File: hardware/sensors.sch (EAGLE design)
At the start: 29 parts, among them J1 CDH, J2 OW, J3 DBG, J4 SUN-UART, J5 ADCS, J6 ENV, J7 SUN, U1 DS18B20, U2 DS18B20, U3 DS18B20

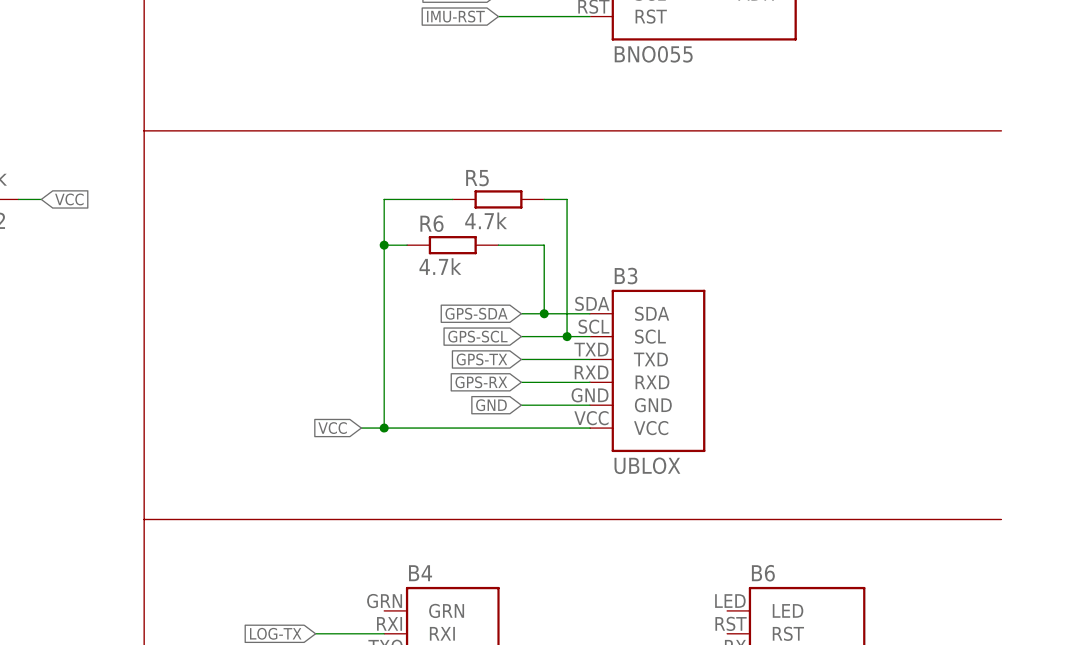
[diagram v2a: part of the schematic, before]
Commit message: Add GPS chip with external antenna
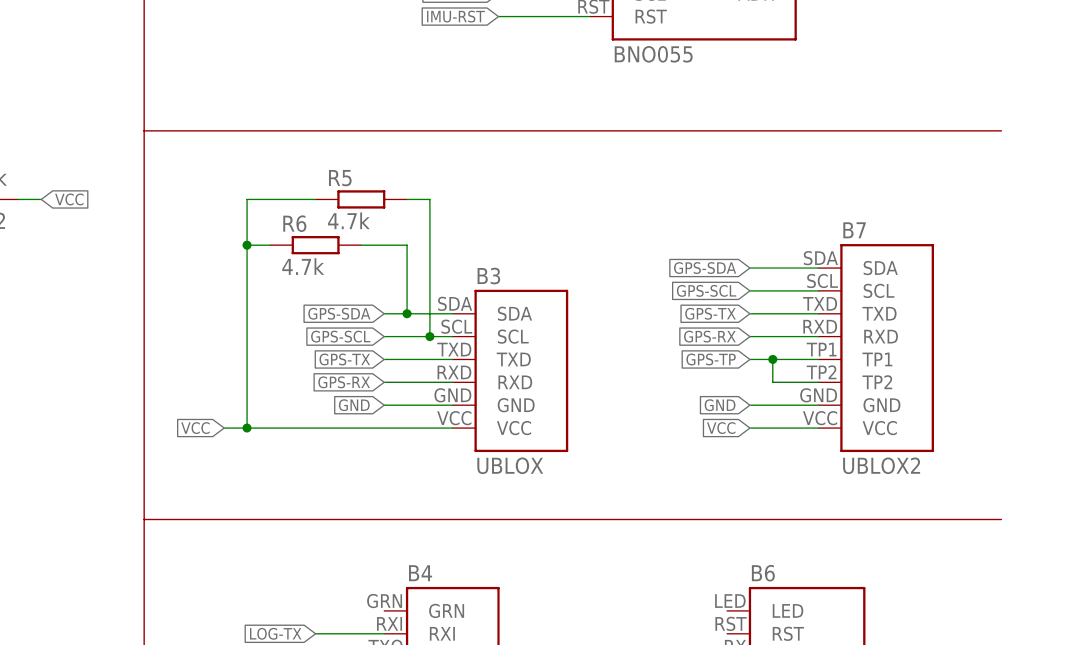
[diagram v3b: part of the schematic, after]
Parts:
- added B7: UBLOX2, Frcy:UPUTRONICS-UBLOX-M8Q
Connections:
- new net GPS-TP: B7.TP1, B7.TP2
- net GND: now also B7.GND
- net GPS-RX: now also B7.RXD
- net GPS-SCL: now also B7.SCL
- net GPS-SDA: now also B7.SDA
- net GPS-TX: now also B7.TXD
- net VCC: now also B7.VCC
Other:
- moved on the sheet: B3, R5, R6
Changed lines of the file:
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@@
 <?xml version="1.0" encoding="utf-8"?>
 <!DOCTYPE eagle SYSTEM "eagle.dtd">
-<eagle version="8.6.0">
+<eagle version="9.0.0">
 <drawing>
 <settings>
@@
 <setting verticaltext="up"/>
 </settings>
-<grid distance="0.1" unitdist="inch" unit="inch" style="lines" multiple="1" display="yes" altdistance="0.05" altunitdist="inch" altunit="inch"/>
+<grid distance="0.1" unitdist="inch" unit="inch" style="lines" multiple="1" display="no" altdistance="0.01" altunitdist="inch" altunit="inch"/>
 <layers>
 <layer number="1" name="Top" color="4" fill="1" visible="no" active="no"/>
@@
 <part name="C10" library="rcl" library_urn="urn:adsk.eagle:library:334" deviceset="C-EU" device="C2012" package3d_urn="urn:adsk.eagle:package:23625/2" value="0.1uF"/>
 <part name="B6" library="Frcy" deviceset="HUAMAO-HM-11" device="BO"/>
+<part name="B7" library="Frcy" deviceset="UPUTRONICS-UBLOX-M8Q" device="" value="UBLOX2"/>
 </parts>
 <sheets>
@@
 <instance part="P+1" gate="VCC" x="144.78" y="33.02"/>
 <instance part="GND1" gate="1" x="144.78" y="17.78"/>
-<instance part="B3" gate="G$1" x="215.9" y="109.22"/>
+<instance part="B3" gate="G$1" x="200.66" y="109.22"/>
 <instance part="B4" gate="G$1" x="195.58" y="76.2"/>
 <instance part="J2" gate="G$1" x="15.24" y="53.34" rot="MR0"/>
@@
 </instance>
 <instance part="U3" gate="G$1" x="43.18" y="116.84"/>
-<instance part="R5" gate="G$1" x="200.66" y="129.54"/>
-<instance part="R6" gate="G$1" x="195.58" y="124.46"/>
+<instance part="R5" gate="G$1" x="185.42" y="129.54"/>
+<instance part="R6" gate="G$1" x="180.34" y="124.46"/>
 <instance part="C1" gate="G$1" x="25.4" y="86.36" rot="R90"/>
 <instance part="C2" gate="G$1" x="25.4" y="58.42" rot="R90"/>
@@
 <instance part="C10" gate="G$1" x="15.24" y="111.76"/>
 <instance part="B6" gate="G$1" x="233.68" y="78.74"/>
+<instance part="B7" gate="G$1" x="241.3" y="114.3"/>
 </instances>
 <busses>
@@
 <segment>
 <pinref part="B3" gate="G$1" pin="VCC"/>
-<wire x1="210.82" y1="104.14" x2="187.96" y2="104.14" width="0.1524" layer="91"/>
-<label x="185.42" y="104.14" size="1.27" layer="95" rot="R180" xref="yes"/>
-<wire x1="187.96" y1="104.14" x2="185.42" y2="104.14" width="0.1524" layer="91"/>
-<wire x1="187.96" y1="104.14" x2="187.96" y2="124.46" width="0.1524" layer="91"/>
-<junction x="187.96" y="104.14"/>
+<wire x1="195.58" y1="104.14" x2="172.72" y2="104.14" width="0.1524" layer="91"/>
+<label x="170.18" y="104.14" size="1.27" layer="95" rot="R180" xref="yes"/>
+<wire x1="172.72" y1="104.14" x2="170.18" y2="104.14" width="0.1524" layer="91"/>
+<wire x1="172.72" y1="104.14" x2="172.72" y2="124.46" width="0.1524" layer="91"/>
+<junction x="172.72" y="104.14"/>
 <pinref part="R6" gate="G$1" pin="1"/>
-<wire x1="187.96" y1="124.46" x2="190.5" y2="124.46" width="0.1524" layer="91"/>
-<wire x1="187.96" y1="124.46" x2="187.96" y2="129.54" width="0.1524" layer="91"/>
-<junction x="187.96" y="124.46"/>
+<wire x1="172.72" y1="124.46" x2="175.26" y2="124.46" width="0.1524" layer="91"/>
+<wire x1="172.72" y1="124.46" x2="172.72" y2="129.54" width="0.1524" layer="91"/>
+<junction x="172.72" y="124.46"/>
 <pinref part="R5" gate="G$1" pin="1"/>
-<wire x1="187.96" y1="129.54" x2="195.58" y2="129.54" width="0.1524" layer="91"/>
+<wire x1="172.72" y1="129.54" x2="180.34" y2="129.54" width="0.1524" layer="91"/>
 </segment>
 <segment>
@@
 <label x="218.44" y="71.12" size="1.27" layer="95" rot="R180" xref="yes"/>
 </segment>
+<segment>
+<wire x1="236.22" y1="104.14" x2="228.6" y2="104.14" width="0.1524" layer="91"/>
+<label x="228.6" y="104.14" size="1.27" layer="95" rot="R180" xref="yes"/>
+<pinref part="B7" gate="G$1" pin="VCC"/>
+</segment>
 </net>
 <net name="GND" class="0">
@@
 <segment>
 <pinref part="B3" gate="G$1" pin="GND"/>
-<wire x1="210.82" y1="106.68" x2="203.2" y2="106.68" width="0.1524" layer="91"/>
-<label x="203.2" y="106.68" size="1.27" layer="95" rot="R180" xref="yes"/>
+<wire x1="195.58" y1="106.68" x2="187.96" y2="106.68" width="0.1524" layer="91"/>
+<label x="187.96" y="106.68" size="1.27" layer="95" rot="R180" xref="yes"/>
 </segment>
 <segment>
@@
 <label x="218.44" y="73.66" size="1.27" layer="95" rot="R180" xref="yes"/>
 </segment>
+<segment>
+<wire x1="236.22" y1="106.68" x2="228.6" y2="106.68" width="0.1524" layer="91"/>
+<label x="228.6" y="106.68" size="1.27" layer="95" rot="R180" xref="yes"/>
+<pinref part="B7" gate="G$1" pin="GND"/>
+</segment>
 </net>
 <net name="IMU-SDA" class="0">
@@
 <segment>
 <pinref part="B3" gate="G$1" pin="SDA"/>
-<wire x1="210.82" y1="116.84" x2="205.74" y2="116.84" width="0.1524" layer="91"/>
-<label x="203.2" y="116.84" size="1.27" layer="95" rot="R180" xref="yes"/>
+<wire x1="195.58" y1="116.84" x2="190.5" y2="116.84" width="0.1524" layer="91"/>
+<label x="187.96" y="116.84" size="1.27" layer="95" rot="R180" xref="yes"/>
 <pinref part="R6" gate="G$1" pin="2"/>
-<wire x1="205.74" y1="116.84" x2="203.2" y2="116.84" width="0.1524" layer="91"/>
-<wire x1="200.66" y1="124.46" x2="205.74" y2="124.46" width="0.1524" layer="91"/>
-<wire x1="205.74" y1="124.46" x2="205.74" y2="116.84" width="0.1524" layer="91"/>
-<junction x="205.74" y="116.84"/>
+<wire x1="190.5" y1="116.84" x2="187.96" y2="116.84" width="0.1524" layer="91"/>
+<wire x1="185.42" y1="124.46" x2="190.5" y2="124.46" width="0.1524" layer="91"/>
+<wire x1="190.5" y1="124.46" x2="190.5" y2="116.84" width="0.1524" layer="91"/>
+<junction x="190.5" y="116.84"/>
 </segment>
 <segment>
@@
 <label x="88.9" y="119.38" size="1.27" layer="95" rot="R180" xref="yes"/>
 </segment>
+<segment>
+<wire x1="236.22" y1="121.92" x2="228.6" y2="121.92" width="0.1524" layer="91"/>
+<label x="228.6" y="121.92" size="1.27" layer="95" rot="R180" xref="yes"/>
+<pinref part="B7" gate="G$1" pin="SDA"/>
+</segment>
 </net>
 <net name="GPS-SCL" class="0">
 <segment>
 <pinref part="B3" gate="G$1" pin="SCL"/>
-<wire x1="210.82" y1="114.3" x2="208.28" y2="114.3" width="0.1524" layer="91"/>
-<label x="203.2" y="114.3" size="1.27" layer="95" rot="R180" xref="yes"/>
+<wire x1="195.58" y1="114.3" x2="193.04" y2="114.3" width="0.1524" layer="91"/>
+<label x="187.96" y="114.3" size="1.27" layer="95" rot="R180" xref="yes"/>
 <pinref part="R5" gate="G$1" pin="2"/>
-<wire x1="208.28" y1="114.3" x2="203.2" y2="114.3" width="0.1524" layer="91"/>
-<wire x1="205.74" y1="129.54" x2="208.28" y2="129.54" width="0.1524" layer="91"/>
-<wire x1="208.28" y1="129.54" x2="208.28" y2="114.3" width="0.1524" layer="91"/>
-<junction x="208.28" y="114.3"/>
+<wire x1="193.04" y1="114.3" x2="187.96" y2="114.3" width="0.1524" layer="91"/>
+<wire x1="190.5" y1="129.54" x2="193.04" y2="129.54" width="0.1524" layer="91"/>
+<wire x1="193.04" y1="129.54" x2="193.04" y2="114.3" width="0.1524" layer="91"/>
+<junction x="193.04" y="114.3"/>
 </segment>
 <segment>
@@
 <wire x1="96.52" y1="116.84" x2="88.9" y2="116.84" width="0.1524" layer="91"/>
 <label x="88.9" y="116.84" size="1.27" layer="95" rot="R180" xref="yes"/>
+</segment>
+<segment>
+<label x="228.6" y="119.38" size="1.27" layer="95" rot="R180" xref="yes"/>
+<wire x1="236.22" y1="119.38" x2="228.6" y2="119.38" width="0.1524" layer="91"/>
+<pinref part="B7" gate="G$1" pin="SCL"/>
 </segment>
 </net>
@@
 <segment>
 <pinref part="B3" gate="G$1" pin="TXD"/>
-<wire x1="210.82" y1="111.76" x2="203.2" y2="111.76" width="0.1524" layer="91"/>
-<label x="203.2" y="111.76" size="1.27" layer="95" rot="R180" xref="yes"/>
+<wire x1="195.58" y1="111.76" x2="187.96" y2="111.76" width="0.1524" layer="91"/>
+<label x="187.96" y="111.76" size="1.27" layer="95" rot="R180" xref="yes"/>
 </segment>
 <segment>
@@
 <label x="76.2" y="53.34" size="1.27" layer="95" xref="yes"/>
 </segment>
+<segment>
+<wire x1="236.22" y1="116.84" x2="228.6" y2="116.84" width="0.1524" layer="91"/>
+<label x="228.6" y="116.84" size="1.27" layer="95" rot="R180" xref="yes"/>
+<pinref part="B7" gate="G$1" pin="TXD"/>
+</segment>
 </net>
 <net name="GPS-RX" class="0">
 <segment>
 <pinref part="B3" gate="G$1" pin="RXD"/>
-<wire x1="210.82" y1="109.22" x2="203.2" y2="109.22" width="0.1524" layer="91"/>
-<label x="203.2" y="109.22" size="1.27" layer="95" rot="R180" xref="yes"/>
+<wire x1="195.58" y1="109.22" x2="187.96" y2="109.22" width="0.1524" layer="91"/>
+<label x="187.96" y="109.22" size="1.27" layer="95" rot="R180" xref="yes"/>
 </segment>
 <segment>
@@
 <label x="76.2" y="55.88" size="1.27" layer="95" xref="yes"/>
 </segment>
+<segment>
+<wire x1="236.22" y1="114.3" x2="228.6" y2="114.3" width="0.1524" layer="91"/>
+<label x="228.6" y="114.3" size="1.27" layer="95" rot="R180" xref="yes"/>
+<pinref part="B7" gate="G$1" pin="RXD"/>
+</segment>
 </net>
 <net name="SPI-CS-SUN" class="0">
@@
 </segment>
 </net>
+<net name="GPS-TP" class="0">
+<segment>
+<pinref part="B7" gate="G$1" pin="TP1"/>
+<wire x1="236.22" y1="111.76" x2="231.14" y2="111.76" width="0.1524" layer="91"/>
+<pinref part="B7" gate="G$1" pin="TP2"/>
+<wire x1="231.14" y1="111.76" x2="228.6" y2="111.76" width="0.1524" layer="91"/>
+<wire x1="236.22" y1="109.22" x2="231.14" y2="109.22" width="0.1524" layer="91"/>
+<wire x1="231.14" y1="109.22" x2="231.14" y2="111.76" width="0.1524" layer="91"/>
+<junction x="231.14" y="111.76"/>
+<label x="228.6" y="111.76" size="1.27" layer="95" rot="R180" xref="yes"/>
+</segment>
+</net>

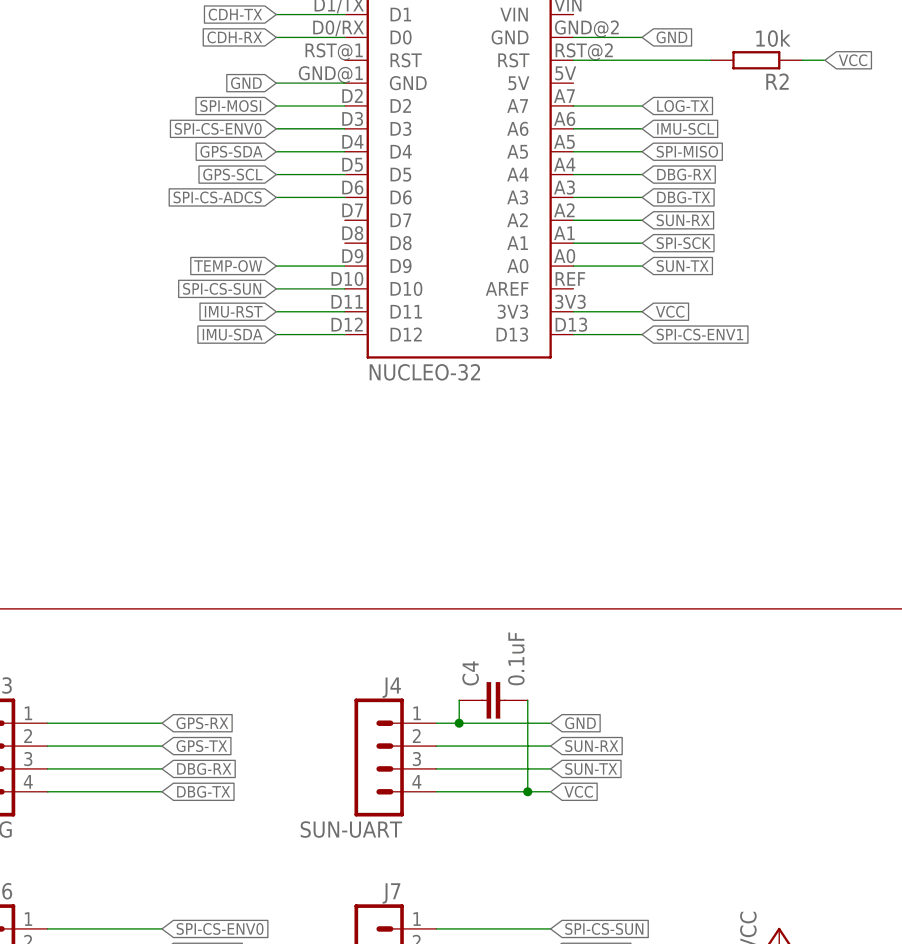
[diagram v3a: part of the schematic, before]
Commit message: Connect external GPS chip on board
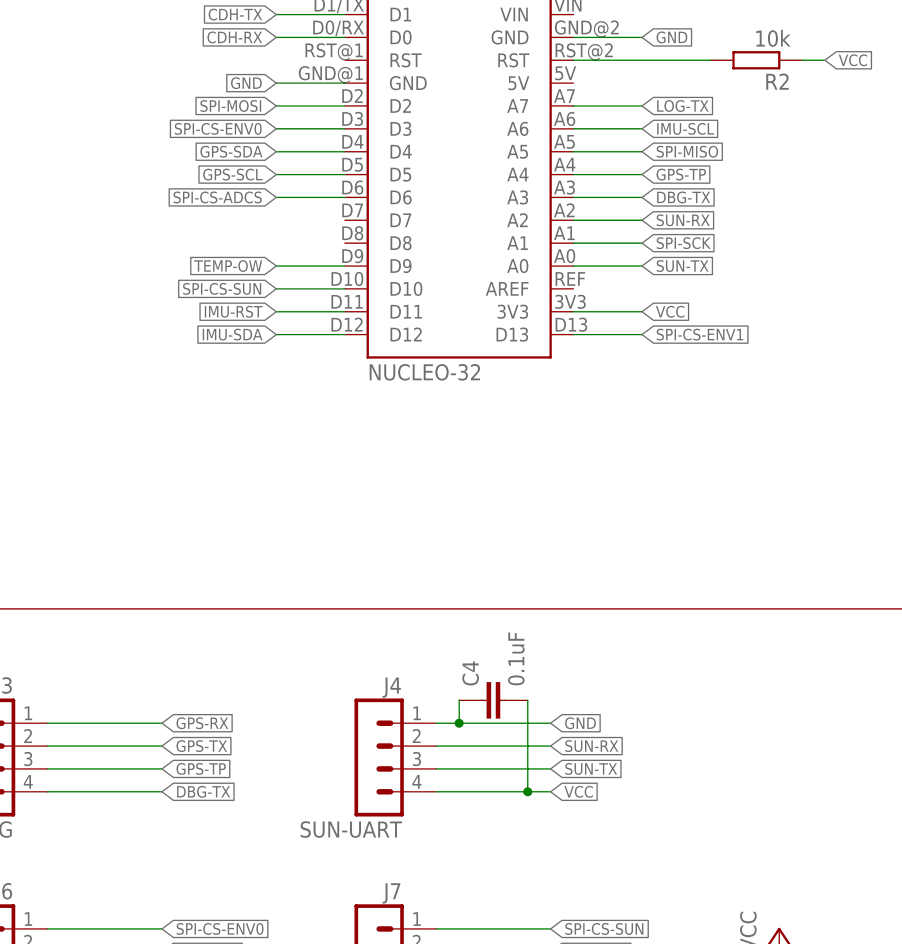
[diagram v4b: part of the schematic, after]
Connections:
- removed net DBG-RX: B1.A4, J3.3
- net GPS-TP: now also B1.A4, J3.3
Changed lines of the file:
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@@
-</segment>
-</net>
-<net name="DBG-RX" class="0">
-<segment>
-<pinref part="J3" gate="G$1" pin="3"/>
-<wire x1="63.5" y1="50.8" x2="76.2" y2="50.8" width="0.1524" layer="91"/>
-<label x="76.2" y="50.8" size="1.27" layer="95" xref="yes"/>
-</segment>
-<segment>
-<pinref part="B1" gate="G$1" pin="A4"/>
-<wire x1="121.92" y1="116.84" x2="129.54" y2="116.84" width="0.1524" layer="91"/>
-<label x="129.54" y="116.84" size="1.27" layer="95" xref="yes"/>
 </segment>
 </net>
@@
 <label x="228.6" y="111.76" size="1.27" layer="95" rot="R180" xref="yes"/>
 </segment>
+<segment>
+<pinref part="J3" gate="G$1" pin="3"/>
+<wire x1="63.5" y1="50.8" x2="76.2" y2="50.8" width="0.1524" layer="91"/>
+<label x="76.2" y="50.8" size="1.27" layer="95" xref="yes"/>
+</segment>
+<segment>
+<pinref part="B1" gate="G$1" pin="A4"/>
+<wire x1="121.92" y1="116.84" x2="129.54" y2="116.84" width="0.1524" layer="91"/>
+<label x="129.54" y="116.84" size="1.27" layer="95" xref="yes"/>
+</segment>
 </net>
